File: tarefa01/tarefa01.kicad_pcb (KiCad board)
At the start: 2 copper layers, 18 parts, among them U1 nrf52832, X1 32MHz, X2 32.768kHz

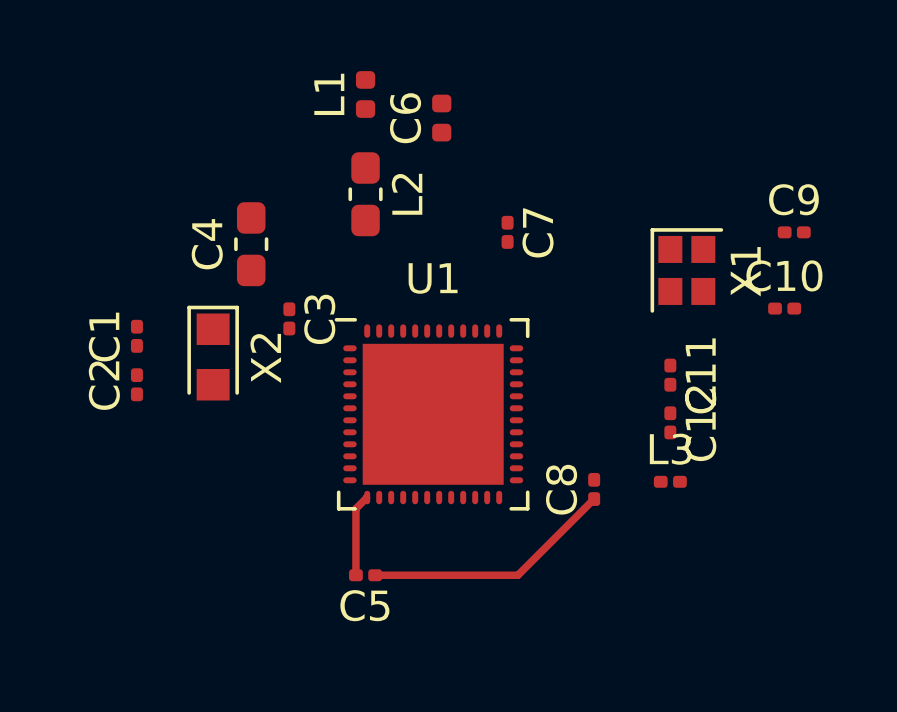
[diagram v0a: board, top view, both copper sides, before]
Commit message: adicionando ground plane
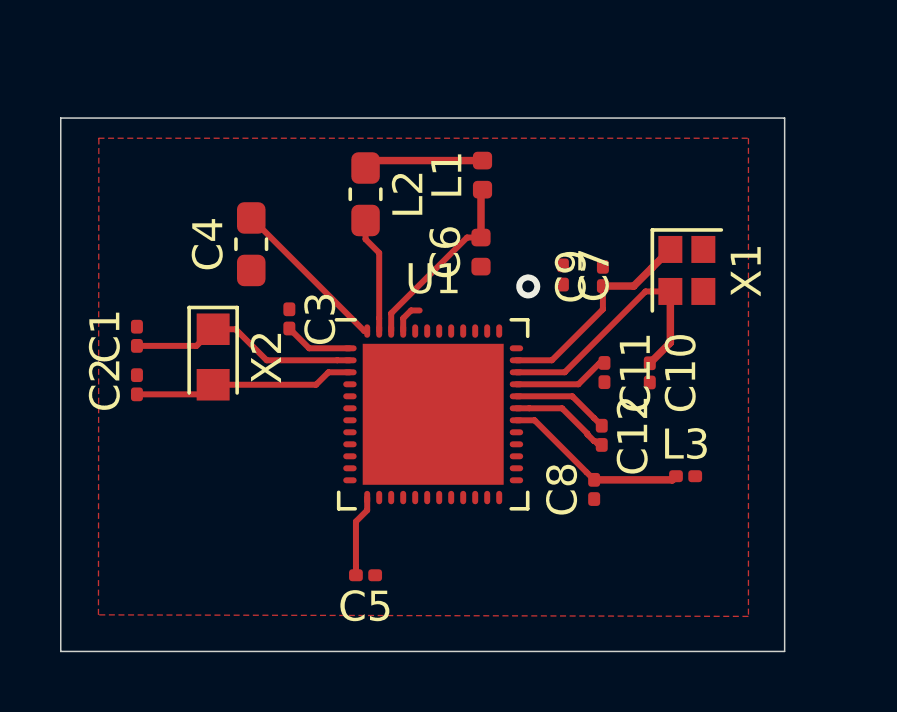
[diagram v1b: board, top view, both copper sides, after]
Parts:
- moved C9 6.55 mm to (150.2, 134.8), turned to 90 degrees
- moved C10 4.98 mm to (151.7, 138.0), turned to 270 degrees
- moved L1 4.74 mm to (146.1, 131.4)
- moved C6 4.66 mm to (146.1, 134.0)
- moved C7 2.33 mm to (148.8, 134.8)
- moved C12 2.32 mm to (150.1, 140.1)
- moved C11 2.20 mm to (150.2, 138.0)
- moved L3 0.54 mm to (152.9, 141.5)
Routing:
- net Net-(C10-Pad1): track 0.00 -> 8.92 mm
- net Net-(C1-Pad1): track 0.00 -> 7.76 mm
- net Net-(C2-Pad1): track 0.00 -> 7.40 mm
- net Net-(C9-Pad1): track 0.00 -> 7.11 mm
- net Net-(C6-Pad2): track 0.00 -> 6.25 mm
- net Net-(C8-Pad2): track 0.00 -> 6.19 mm
- net VDD: track 2.73 -> 8.17 mm, vias 0 -> 1
- net Net-(L1-Pad2): track 0.00 -> 4.00 mm
- net Earth: track 8.35 -> 4.45 mm
- net Net-(L2-Pad2): track 0.00 -> 3.87 mm
- net Net-(C12-Pad1): track 0.00 -> 3.25 mm
- net Net-(C11-Pad1): track 0.00 -> 3.23 mm
- net Net-(C3-Pad2): track 0.00 -> 2.29 mm
- added copper zone on F.Cu, net Earth
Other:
- board outline added: 24.1 x 17.8 mm
- net class Default: clearance 0.2 -> 0.18
- rule trace_clearance: 0.2 -> 0.18

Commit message: Projeto finalizado
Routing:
- net Earth: track 4.45 -> 8.29 mm, vias 0 -> 2
- net VDD: track 8.17 -> 9.88 mm, vias 1 -> 6
- added copper zone on B.Cu, net Earth
- added copper zone on B.Cu, net VDD
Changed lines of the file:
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@@
-(kicad_pcb (version 20171130) (host pcbnew 5.1.2-f72e74a~84~ubuntu18.04.1)
+(kicad_pcb (version 20171130) (host pcbnew 5.1.2-f72e74a~84~ubuntu16.04.1)
   (general
     (thickness 1.6)
     (drawings 4)
-    (tracks 65)
+    (tracks 89)
     (zones 0)
     (modules 18)
@@
     (34 B.Paste user)
     (35 F.Paste user)
-    (36 B.SilkS user)
+    (36 B.SilkS user hide)
     (37 F.SilkS user)
     (38 B.Mask user)
-    (39 F.Mask user)
+    (39 F.Mask user hide)
     (40 Dwgs.User user)
     (41 Cmts.User user)
@@
   (segment (start 149.63399 140.084408) (end 149.63399 140.05819) (width 0.2) (layer F.Cu) (net 1))
   (segment (start 149.856592 140.30701) (end 149.63399 140.084408) (width 0.2) (layer F.Cu) (net 1))
-  (segment (start 149.63399 140.05819) (end 148.790801 139.215001) (width 0.2) (layer F.Cu) (net 1))
+  (via (at 148.975067 139.619733) (size 0.6) (drill 0.3) (layers F.Cu B.Cu) (net 1))
+  (segment (start 149.439742 140.084408) (end 148.975067 139.619733) (width 0.25) (layer F.Cu) (net 1))
+  (segment (start 149.63399 140.084408) (end 149.439742 140.084408) (width 0.25) (layer F.Cu) (net 1))
+  (segment (start 148.790801 139.435467) (end 148.790801 139.220011) (width 0.25) (layer F.Cu) (net 1))
+  (segment (start 149.439742 140.084408) (end 148.790801 139.435467) (width 0.25) (layer F.Cu) (net 1))
+  (segment (start 148.675068 139.319734) (end 146.736534 139.319734) (width 0.25) (layer B.Cu) (net 1))
+  (segment (start 148.975067 139.619733) (end 148.675068 139.319734) (width 0.25) (layer B.Cu) (net 1))
+  (via (at 146.257501 138.827501) (size 0.6) (drill 0.3) (layers F.Cu B.Cu) (net 1))
+  (segment (start 146.257501 138.840701) (end 146.257501 138.827501) (width 0.25) (layer B.Cu) (net 1))
+  (segment (start 146.736534 139.319734) (end 146.257501 138.840701) (width 0.25) (layer B.Cu) (net 1))
   (segment (start 136.605 137.135) (end 137.16 136.58) (width 0.2) (layer F.Cu) (net 2))
   (segment (start 134.62 137.135) (end 136.605 137.135) (width 0.2) (layer F.Cu) (net 2))
@@
   (segment (start 140.360001 137.215001) (end 141.720001 137.215001) (width 0.2) (layer F.Cu) (net 4))
   (segment (start 139.7 136.555) (end 140.360001 137.215001) (width 0.2) (layer F.Cu) (net 4))
-  (segment (start 141.92 144.48) (end 141.92 144.78) (width 0.2) (layer F.Cu) (net 5))
-  (segment (start 141.92 142.990002) (end 141.92 144.48) (width 0.2) (layer F.Cu) (net 5))
-  (segment (start 142.295001 142.615001) (end 141.92 142.990002) (width 0.2) (layer F.Cu) (net 5))
+  (segment (start 138.43 132.87) (end 139.9895 134.4295) (width 0.2) (layer F.Cu) (net 5))
+  (via (at 139.9895 134.4295) (size 0.6) (drill 0.3) (layers F.Cu B.Cu) (net 5))
+  (via (at 141.2367 135.4709) (size 0.6) (drill 0.3) (layers F.Cu B.Cu) (net 5))
+  (segment (start 142.295001 136.640001) (end 142.295001 136.515001) (width 0.2) (layer F.Cu) (net 5))
+  (segment (start 142.295001 136.515001) (end 141.2509 135.4709) (width 0.2) (layer F.Cu) (net 5))
+  (segment (start 147.695001 137.215001) (end 148.5138 136.396202) (width 0.2) (layer F.Cu) (net 5))
+  (segment (start 147.270001 137.215001) (end 147.695001 137.215001) (width 0.2) (layer F.Cu) (net 5))
+  (via (at 148.5138 136.2837) (size 0.6) (drill 0.3) (layers F.Cu B.Cu) (net 5))
+  (segment (start 148.5138 136.396202) (end 148.5138 136.2837) (width 0.2) (layer F.Cu) (net 5))
+  (segment (start 148.5186 135.0903) (end 148.5182 135.0899) (width 0.2) (layer F.Cu) (net 5))
+  (segment (start 148.8186 135.0903) (end 148.5186 135.0903) (width 0.2) (layer F.Cu) (net 5))
+  (via (at 147.8153 135.0899) (size 0.6) (drill 0.3) (layers F.Cu B.Cu) (net 5))
+  (segment (start 148.5182 135.0899) (end 147.8153 135.0899) (width 0.2) (layer F.Cu) (net 5))
+  (segment (start 141.92 144.48) (end 141.9225 144.4775) (width 0.2) (layer F.Cu) (net 5))
+  (segment (start 141.92 144.78) (end 141.92 144.48) (width 0.2) (layer F.Cu) (net 5))
+  (via (at 141.9225 143.8783) (size 0.6) (drill 0.3) (layers F.Cu B.Cu) (net 5))
+  (segment (start 141.9225 144.4775) (end 141.9225 143.8783) (width 0.2) (layer F.Cu) (net 5))
+  (segment (start 141.9225 143.8783) (end 141.9225 142.7226) (width 0.2) (layer B.Cu) (net 5))
+  (segment (start 141.9225 142.7226) (end 142.2654 142.3797) (width 0.2) (layer B.Cu) (net 5))
+  (segment (start 142.295001 142.615001) (end 142.0114 142.898602) (width 0.2) (layer F.Cu) (net 5))
   (segment (start 142.295001 142.190001) (end 142.295001 142.615001) (width 0.2) (layer F.Cu) (net 5))
-  (segment (start 142.200001 136.640001) (end 142.295001 136.640001) (width 0.2) (layer F.Cu) (net 5))
-  (segment (start 138.43 132.87) (end 142.200001 136.640001) (width 0.2) (layer F.Cu) (net 5))
-  (via (at 147.6629 135.1534) (size 0.8) (drill 0.4) (layers F.Cu B.Cu) (net 5))
+  (via (at 142.0114 142.898602) (size 0.6) (drill 0.3) (layers F.Cu B.Cu) (net 5))
   (segment (start 146.0881 131.9784) (end 146.1389 131.9276) (width 0.25) (layer F.Cu) (net 6))
   (segment (start 146.0881 133.523) (end 146.0881 131.9784) (width 0.25) (layer F.Cu) (net 6))
@@
       )
     )
+  )
+  (zone (net 5) (net_name VDD) (layer B.Cu) (hatch edge 0.508)
+    (connect_pads (clearance 0.238))
+    (min_thickness 0.254)
+    (fill yes (arc_segments 32) (thermal_gap 0.408) (thermal_bridge_width 0.508))
+    (polygon
+      (pts
+        (xy 154.94 137.795) (xy 154.94 130.175) (xy 133.35 130.175) (xy 133.35 146.05) (xy 154.94 146.05)
+      )
+    )
+  )
+  (zone (net 1) (net_name Earth) (layer B.Cu) (hatch edge 0.508)
+    (priority 1)
+    (connect_pads (clearance 0.238))
+    (min_thickness 0.254)
+    (fill yes (arc_segments 32) (thermal_gap 0.508) (thermal_bridge_width 0.508))
+    (polygon
+      (pts
+        (xy 149.86 140.97) (xy 149.86 137.795) (xy 145.415 137.795) (xy 145.415 140.97)
+      )
+    )
+  )
+  (zone (net 1) (net_name Earth) (layer B.Cu) (hatch edge 0.508)
+    (priority 1)
+    (connect_pads (clearance 0.238))
+    (min_thickness 0.254)
+    (fill yes (arc_segments 32) (thermal_gap 0.508) (thermal_bridge_width 0.508))
+    (polygon
+      (pts
+        (xy 150.495 140.335) (xy 150.495 138.43) (xy 145.415 138.43) (xy 145.415 140.335)
+      )
+    )
